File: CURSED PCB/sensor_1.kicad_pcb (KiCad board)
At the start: 4 copper layers, 40 x 40 mm, 68 parts, among them J1 Programming Header, J2 Micro_SD_Card, J3 2 Wire Block for laser, J4 2 Wire Block for PZT, J5 G125-MH104M4-04AD000P, U1 MIC94090YC6, U10 MCP2562, U11 TPS61046YFF, U12 AD5761BRUZ, U2 INA180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

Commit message: fix
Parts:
- F1: value 1A -> 1.5A
- R1, R2, R3: value 22R -> 220R
- R14, R4, R5: value 22R -> 10k
- R6: value 165m -> 198m
- Y1: value 24Hz crystal -> 24MHz crystal
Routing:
- net Net-(D4-K): track 14.2 -> 10.9 mm
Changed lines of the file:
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@@
 			)
 		)
-		(property "Value" "22R"
+		(property "Value" "220R"
 			(at 0 1.43 90)
 			(layer "F.Fab")
@@
 			(net 59 "unconnected-(U3-PA8-Pad18)")
 			(pinfunction "PA8")
-			(pintype "bidirectional")
+			(pintype "bidirectional+no_connect")
 			(solder_mask_margin 0.102)
 		)
@@
 			(net 60 "unconnected-(U3-PA12-Pad22)")
 			(pinfunction "PA12")
-			(pintype "bidirectional")
+			(pintype "bidirectional+no_connect")
 			(solder_mask_margin 0.102)
 		)
@@
 			)
 		)
-		(property "Value" "165m"
+		(property "Value" "198m"
 			(at 0 1.43 0)
 			(layer "F.Fab")
@@
 			)
 		)
-		(property "Value" "22R"
+		(property "Value" "220R"
 			(at 0 1.43 90)
 			(layer "F.Fab")
@@
 			)
 		)
-		(property "Value" "1A"
+		(property "Value" "1.5A"
 			(at 2.55 3.1 0)
 			(layer "F.Fab")
@@
 			)
 		)
-		(property "Value" "22R"
+		(property "Value" "220R"
 			(at 0 1.43 90)
 			(layer "F.Fab")
@@
 			)
 		)
-		(property "Value" "22R"
+		(property "Value" "10k"
 			(at 0 -1.43 0)
 			(layer "B.Fab")
@@
 			)
 		)
-		(property "Value" "24Hz crystal"
+		(property "Value" "24MHz crystal"
 			(at -0.2 -3.35 180)
 			(layer "B.Fab")
@@
 		(tags "MLF1608E120JTD25 ")
 		(property "Reference" "L1"
-			(at -23.7 1.6 0)
+			(at 1.6698 1.6 0)
 			(unlocked yes)
 			(layer "B.SilkS")
@@
 			)
 		)
-		(property "Value" "22R"
+		(property "Value" "10k"
 			(at 0 -1.43 0)
 			(layer "B.Fab")
@@
 			)
 		)
-		(property "Value" "22R"
+		(property "Value" "10k"
 			(at 0 -1.43 0)
 			(layer "B.Fab")
@@
 	)
 	(segment
-		(start 32.9 46.96)
-		(end 34.8 45.06)
-		(width 0.2)
-		(layer "F.Cu")
-		(net 11)
-	)
-	(segment
-		(start 34.8 45.06)
-		(end 34.8 44.5)
-		(width 0.2)
-		(layer "F.Cu")
-		(net 11)
-	)
-	(segment

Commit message: redone pcb
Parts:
- added C16: 0.1uF, Capacitor_SMD:C_0805_2012Metric_Pad1.18x1.45mm_HandSolder, F.Cu at (43.9, 55.4)
- added C21: 10uF, Capacitor_SMD:C_0805_2012Metric_Pad1.18x1.45mm_HandSolder, F.Cu at (43.9, 58.1)
- added C22: 0.1uF, Capacitor_SMD:C_0805_2012Metric_Pad1.18x1.45mm_HandSolder, F.Cu at (57.6, 52.7)
- added C23: 10uF, Capacitor_SMD:C_0805_2012Metric_Pad1.18x1.45mm_HandSolder, F.Cu at (57.6, 54.9)
- C1, C11, C12, C19, C20, C3, C4, C5, C6, C8: footprint Capacitor_SMD:C_0603_1608Metric_Pad1.08x0.95mm_HandSolder -> Capacitor_SMD:C_0805_2012Metric_Pad1.18x1.45mm_HandSolder
- C10, C13, C2, C7, C9: footprint Capacitor_SMD:C_0603_1608Metric_Pad1.08x0.95mm_HandSolder -> Capacitor_SMD:C_0805_2012Metric_Pad1.18x1.45mm_HandSolder; moved to B.Cu
- C14, C15, C17, C18: footprint Capacitor_SMD:C_0603_1608Metric_Pad1.08x0.95mm_HandSolder -> Capacitor_SMD:C_0805_2012Metric_Pad1.18x1.45mm_HandSolder; moved to F.Cu
- D1, D2, D3: footprint LED_SMD:LED_0603_1608Metric_Pad1.05x0.95mm_HandSolder -> LED_SMD:LED_0805_2012Metric_Pad1.15x1.40mm_HandSolder; moved to B.Cu
- D4: footprint OptoDevice:Osram_DIL2_4.3x4.65mm_P5.08mm -> Package_TO_SOT_THT:TO-5-3; moved to F.Cu
- H1, H2, H3, H4: footprint MountingHole:MountingHole_2.2mm_M2_DIN965_Pad -> MountingHole:MountingHole_3.2mm_M3_DIN965_Pad
- J1: value Programming Header -> Conn_02x07_Odd_Even; footprint canhw_footprints:PinSocket_5x2.54_SMD_90deg_952-3198-1-ND -> Connector_PinHeader_1.27mm:PinHeader_2x07_P1.27mm_Vertical_SMD
- JP2, U12, U3, U5: moved to B.Cu
- R1, R2, R3: footprint Resistor_SMD:R_0603_1608Metric_Pad0.98x0.95mm_HandSolder -> Resistor_SMD:R_0805_2012Metric_Pad1.20x1.40mm_HandSolder; moved to B.Cu
- R10, R11, R7, R8, R9: footprint Resistor_SMD:R_0603_1608Metric_Pad0.98x0.95mm_HandSolder -> Resistor_SMD:R_0805_2012Metric_Pad1.20x1.40mm_HandSolder; moved to F.Cu
- R12, R13, R14, R4, R5, R6: footprint Resistor_SMD:R_0603_1608Metric_Pad0.98x0.95mm_HandSolder -> Resistor_SMD:R_0805_2012Metric_Pad1.20x1.40mm_HandSolder
- TP1, TP2, TP3, TP4, TP5, TP6: footprint TestPoint:TestPoint_Loop_D2.50mm_Drill1.0mm -> TestPoint:TestPoint_Pad_1.5x1.5mm
- U6, U7, U8: moved to F.Cu
- moved TP2 42.4 mm to (70.0, 57.0), turned to 0 degrees
- moved C12 37.6 mm to (69.9, 52.7), turned to -90 degrees
- moved C11 36.8 mm to (67.3, 56.7), turned to -90 degrees
- moved U4 34.6 mm to (66.0, 52.7)
- moved R12 33.3 mm to (31.4, 48.7), turned to 90 degrees
- moved C19 31.8 mm to (38.4, 52.7)
- moved U11 31.8 mm to (37.3, 48.3)
- moved R13 29.8 mm to (34.5, 48.6), turned to -90 degrees
- moved L1 28.8 mm to (39.8, 47.8), turned to -90 degrees
- moved C8 25.6 mm to (61.9, 49.6), turned to 90 degrees
- moved C20 24.5 mm to (35.4, 52.6)
- moved C6 20.6 mm to (54.8, 60.1)
- moved TP3 19.6 mm to (42.9, 41.2), turned to 0 degrees
- moved C3 19.2 mm to (49.7, 45.6)
- moved R6 18.3 mm to (56.3, 40.0), turned to 0 degrees
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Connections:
- C10 pad 2: GND -> AGND
- C13 pad 2: GND -> AGND
- C14 pad 2: 5V -> +5V
- C15 pad 1: Net-(D4-K) -> Net-(D4-Cathode_2)
- C18 pad 2: GND -> AGND
- C19 pad 2: GND -> AGND
- C20 pad 2: GND -> AGND
- C3 pad 1: GND -> AGND
- C7 pad 2: GND -> AGND
- C9 pad 2: GND -> AGND
- D4 pad 1: Net-(D4-K) -> Net-(D4-Cathode_2)
- D4 pad 2: GND -> AGND
- H2 pad 1: GND -> AGND
- J1 pad 1: /PGC/ICSPDAT -> unconnected-(J1-Pin_1-Pad1)
- J1 pad 2: /PGD/ICSPCLK -> unconnected-(J1-Pin_2-Pad2)
- J1 pad 3: +3.3VD -> unconnected-(J1-Pin_3-Pad3)
- J1 pad 4: GND -> /PGC/ICSPDAT
- J1 pad 5: /MCLR -> unconnected-(J1-Pin_5-Pad5)
- J2 pad 2: Net-(J2-DAT3/CD) -> /CS2
- J2 pad 3: Net-(J2-CMD) -> /MOSI
- J2 pad 7: Net-(J2-DAT0) -> /MISO
- R12 pad 1: GND -> AGND
- R14 pad 1: /CS2 -> +3.3VD
- R14 pad 2: Net-(J2-DAT3/CD) -> /CS2
- R4 pad 1: /MOSI -> +3.3VD
- R4 pad 2: Net-(J2-CMD) -> /MOSI
- R5 pad 1: /MISO -> +3.3VD
- R5 pad 2: Net-(J2-DAT0) -> /MISO
- R7 pad 1: 5V -> +5V
- R8 pad 1: 5V -> +5V
- R9 pad 1: Net-(D4-K) -> Net-(D4-Cathode_2)
- U11 pad 1: GND -> AGND
- U11 pad 7: GND -> AGND
- U3 pad 14: GND -> AGND
- U5 pad 1: GND -> AGND
- U6 pad 2: GND -> AGND
- U6 pad 4: Net-(D4-K) -> Net-(D4-Cathode_2)
- U6 pad 5: 5V -> +5V
- U7 pad 2: GND -> AGND
- U7 pad 3: GND -> AGND
- U8 pad 2: GND -> AGND
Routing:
- net +5V: track 36.1 -> 112.6 mm, vias 7 -> 13
- net /MOSI: track 27.4 -> 90.1 mm, vias 1 -> 3
- net /MISO: track 23.8 -> 84.6 mm, vias 0 -> 4
- net +3.3VA: track 124.4 -> 76.4 mm, vias 4 -> 5
- net AGND: track 0.00 -> 43.3 mm, vias 0 -> 19
- net +3.3VD: track 109.4 -> 74.0 mm, vias 4 -> 14
- net /CS2: track 6.06 -> 32.1 mm, vias 1 -> 2
- net Net-(D4-Cathode_2): track 0.00 -> 22.1 mm
- net /SCLK: track 33.2 -> 54.9 mm, vias 3 -> 4
- net /Las_enable: track 42.4 -> 21.4 mm
- net 5V: track 19.5 -> 0.00 mm, vias 2 -> 0
- net Net-(JP4-B): track 2.26 -> 19.3 mm, vias 0 -> 2
- net /Amplifer/anti-aliasing filter/VIN: track 27.8 -> 12.0 mm, vias 2 -> 0
- net /MCLR: track 18.5 -> 34.2 mm
- net /CS_DAC: track 7.98 -> 21.3 mm
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- added copper zone on In1.Cu, net +3.3VD
- added copper zone on In2.Cu, net AGND
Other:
- board size 40 x 40 mm -> 42 x 40 mm

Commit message: wires
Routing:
- net GND: vias 27 -> 26
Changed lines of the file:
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@@
+	)
+	(via
+		(at 44.75 46.85)
+		(size 0.6)
+		(drill 0.3)
+		(layers "F.Cu" "B.Cu")
+		(net 1)
 	)
 	(via
@@
 	)
 	(via
-		(at 44.75 46.85)
-		(size 0.6)
-		(drill 0.3)
-		(layers "F.Cu" "B.Cu")
-		(net 1)
-	)
-	(via
 		(at 71.07 41.87)
 		(size 0.6)
@@
 		(layers "F.Cu" "B.Cu")
 		(free yes)
-		(net 1)
-	)
-	(via
-		(at 44.75 46.85)
-		(size 0.6)
-		(drill 0.3)
-		(layers "F.Cu" "B.Cu")
 		(net 1)
 	)
@@
 	)
 	(segment
-		(start 44.6 47.6)
-		(end 44.6 47)
-		(width 0.381)
-		(layer "B.Cu")
-		(net 1)
-	)
-	(segment
 		(start 54.8 61.1375)
 		(end 55.6375 61.1375)
@@
 	)
 	(segment
-		(start 44.6 47)
-		(end 44.75 46.85)
+		(start 44.75 46.85)
+		(end 44.75 47.45)
 		(width 0.381)
 		(layer "B.Cu")
@@
 	)
 	(segment
+		(start 44.75 47.45)
+		(end 44.6 47.6)
+		(width 0.381)
+		(layer "B.Cu")
+		(net 1)
+	)
+	(segment
 		(start 56.5334 52.6166)
 		(end 56.5334 52.6431)
@@
 	)
 	(segment
-		(start 44.75 46.85)
-		(end 45.343055 46.85)
-		(width 0.381)
-		(layer "In2.Cu")
-		(net 1)
-	)
-	(segment
 		(start 46.9553 48.462245)
 		(end 46.9553 49.037755)
@@
 		(width 0.381)
 		(layer "In2.Cu")
+		(net 1)
+	)
+	(segment
+		(start 45.343055 46.85)
+		(end 44.75 46.85)
+		(width 0.381)
+		(layer "In2.Cu")

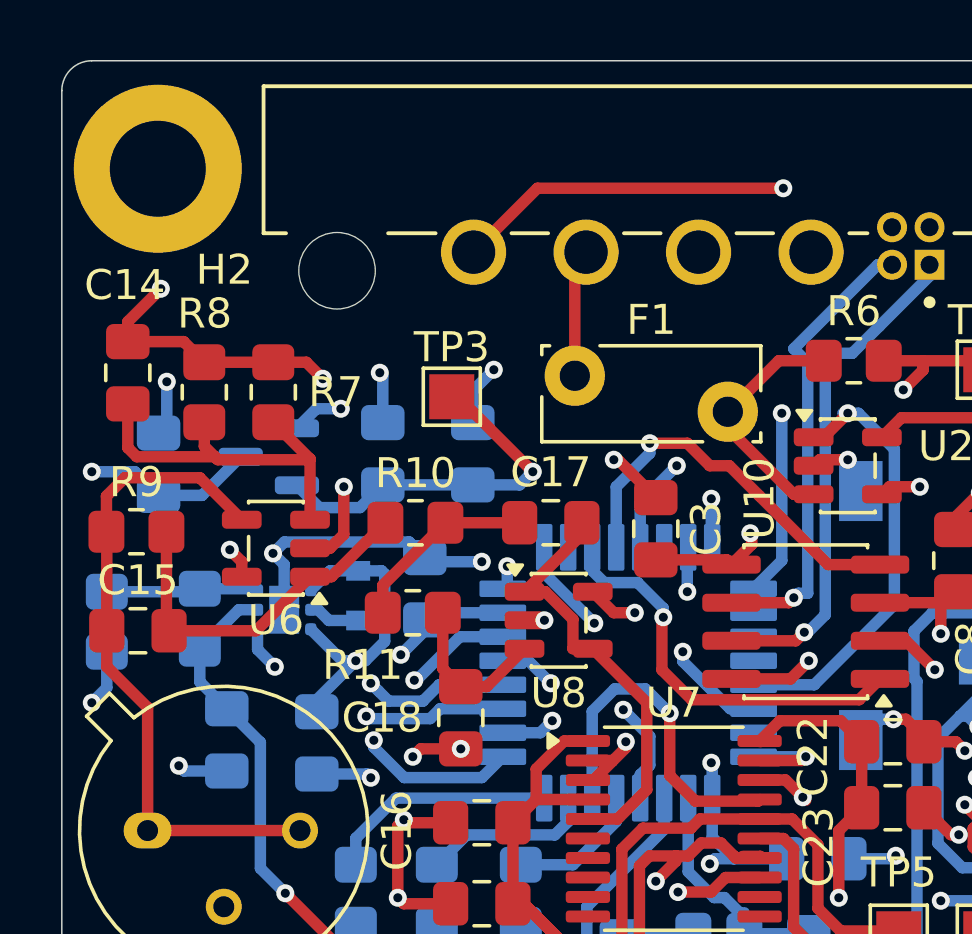
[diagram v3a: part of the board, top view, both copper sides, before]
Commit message: no spilt-ground plane (bad idea)
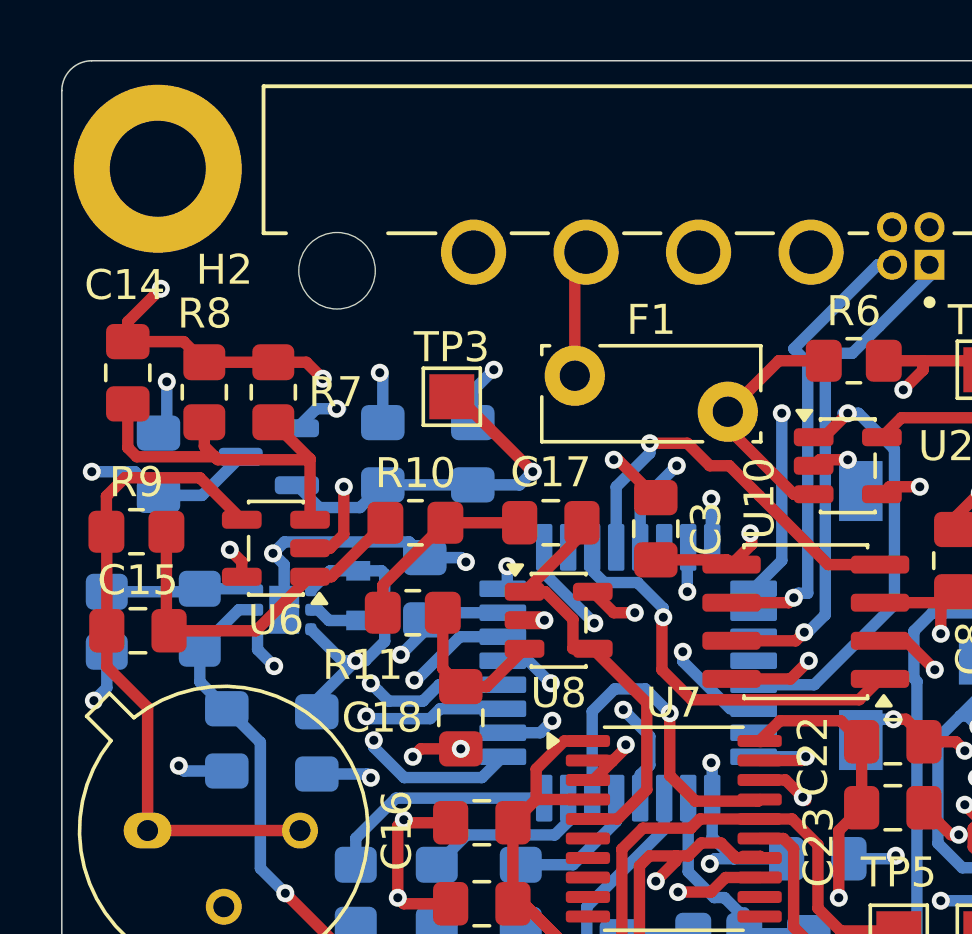
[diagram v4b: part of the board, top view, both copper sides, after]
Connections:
- C10 pad 2: AGND -> GND
- C13 pad 2: AGND -> GND
- C16 pad 2: AGND -> GND
- C18 pad 2: AGND -> GND
- C19 pad 2: AGND -> GND
- C20 pad 2: AGND -> GND
- C21 pad 2: AGND -> GND
- C3 pad 1: AGND -> GND
- C7 pad 2: AGND -> GND
- C9 pad 2: AGND -> GND
- D4 pad 2: AGND -> GND
- H2 pad 1: AGND -> GND
- R12 pad 1: AGND -> GND
- U11 pad 1: AGND -> GND
- U11 pad 7: AGND -> GND
- U3 pad 14: AGND -> GND
- U5 pad 1: AGND -> GND
- U6 pad 2: AGND -> GND
- U7 pad 2: AGND -> GND
- U7 pad 3: AGND -> GND
- U8 pad 2: AGND -> GND
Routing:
- net AGND: track 43.3 -> 0.00 mm, vias 19 -> 0
- net GND: track 93.9 -> 108.9 mm, vias 26 -> 44
- removed copper zone on In2.Cu, net AGND

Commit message: adressing koby thing
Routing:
- net GND: track 108.9 -> 43.9 mm, vias 44 -> 3
- net +5V: track 112.6 -> 91.5 mm, vias 13 -> 14
- net /CS_DAC: track 21.3 -> 36.3 mm
- net (no net): track 0.00 -> 8.68 mm
- net /MISO: track 84.6 -> 76.7 mm
- net /MOSI: track 90.1 -> 83.2 mm, vias 3 -> 4
- net /CS2: track 32.1 -> 31.5 mm
- net /CS: track 28.4 -> 27.8 mm, vias 4 -> 2
- net /Power/CANH: track 17.1 -> 16.6 mm
- net /SCLK: track 54.9 -> 55.2 mm, vias 4 -> 3
- added copper zone on B.Cu, net GND
- added copper zone on F.Cu, net GND

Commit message: grounding stuff
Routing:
- net GND: track 43.9 -> 62.0 mm, vias 3 -> 6
- net (no net): track 8.68 -> 0.00 mm
- net /SCLK: track 55.2 -> 54.1 mm, vias 3 -> 4

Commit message: h
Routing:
- net (no net): track 0.00 -> 2.39 mm
- net GND: vias 6 -> 5

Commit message: smell error
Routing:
- net +5V: track 91.4 -> 84.4 mm
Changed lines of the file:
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@@
-	)
-	(segment
-		(start 38.6 40.6)
-		(end 35.5 43.7)
-		(width 0.381)
-		(layer "In2.Cu")
-		(net 3)
-	)
-	(segment
-		(start 35.5 43.7)
-		(end 35.5 46.3)
-		(width 0.381)
-		(layer "In2.Cu")
-		(net 3)
 	)
 	(segment
